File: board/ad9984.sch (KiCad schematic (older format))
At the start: 39 parts, among them P401 AD9984 I2C, U401 AD9984

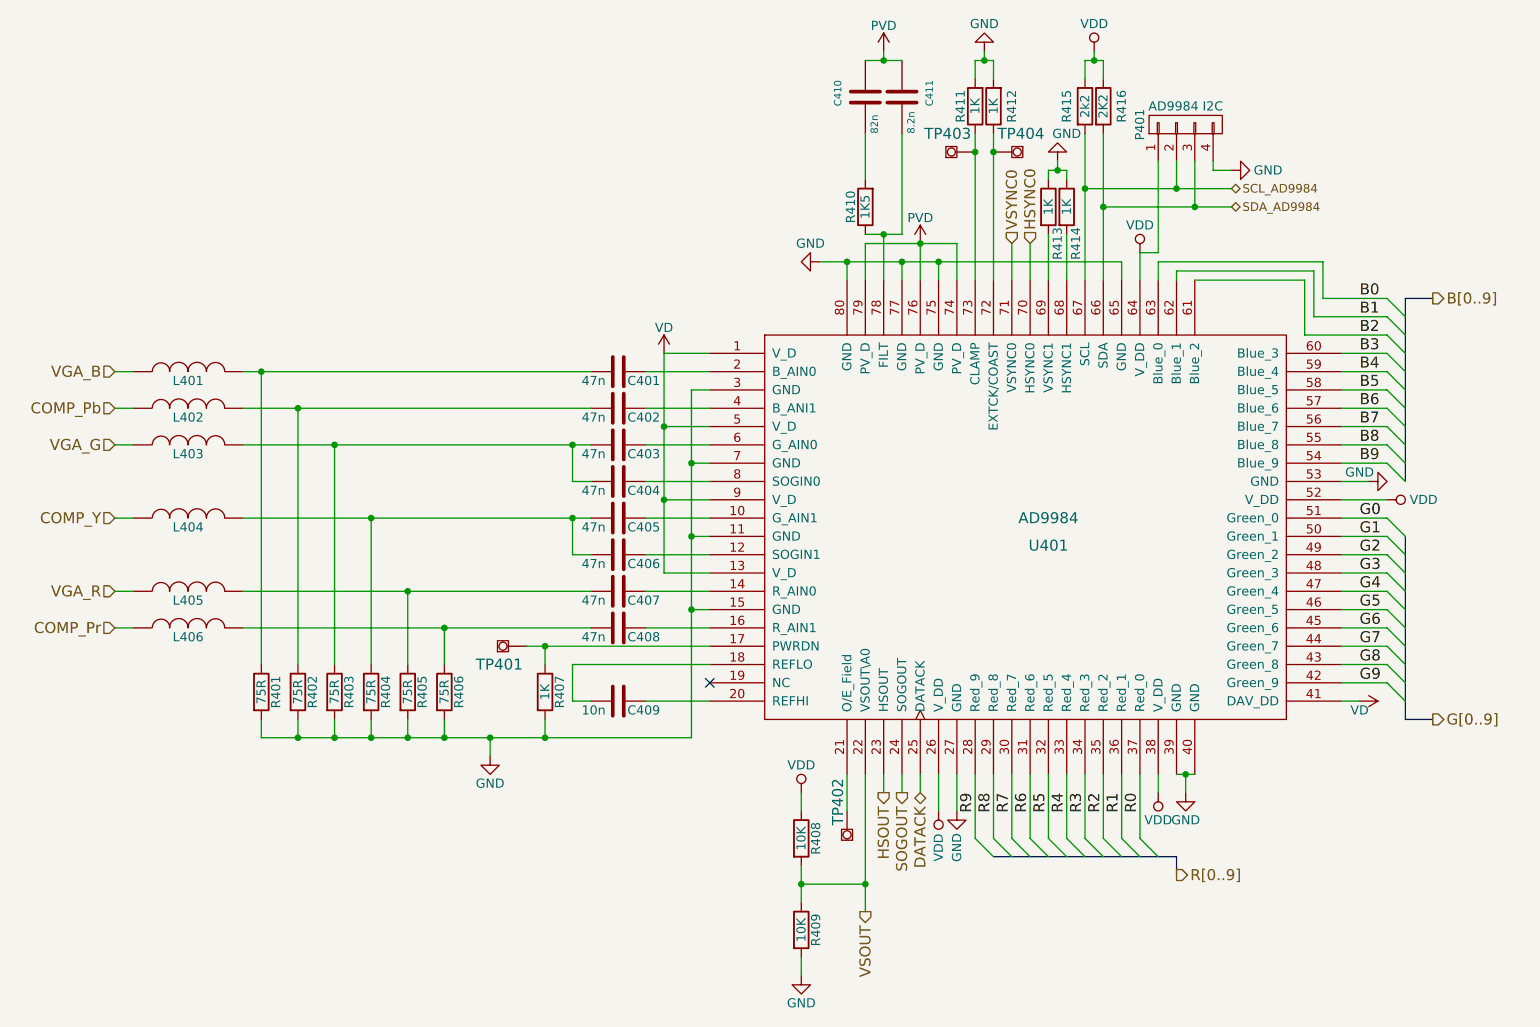
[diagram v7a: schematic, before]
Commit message: Remove component input to allow design to fit on smaller and much cheaper board
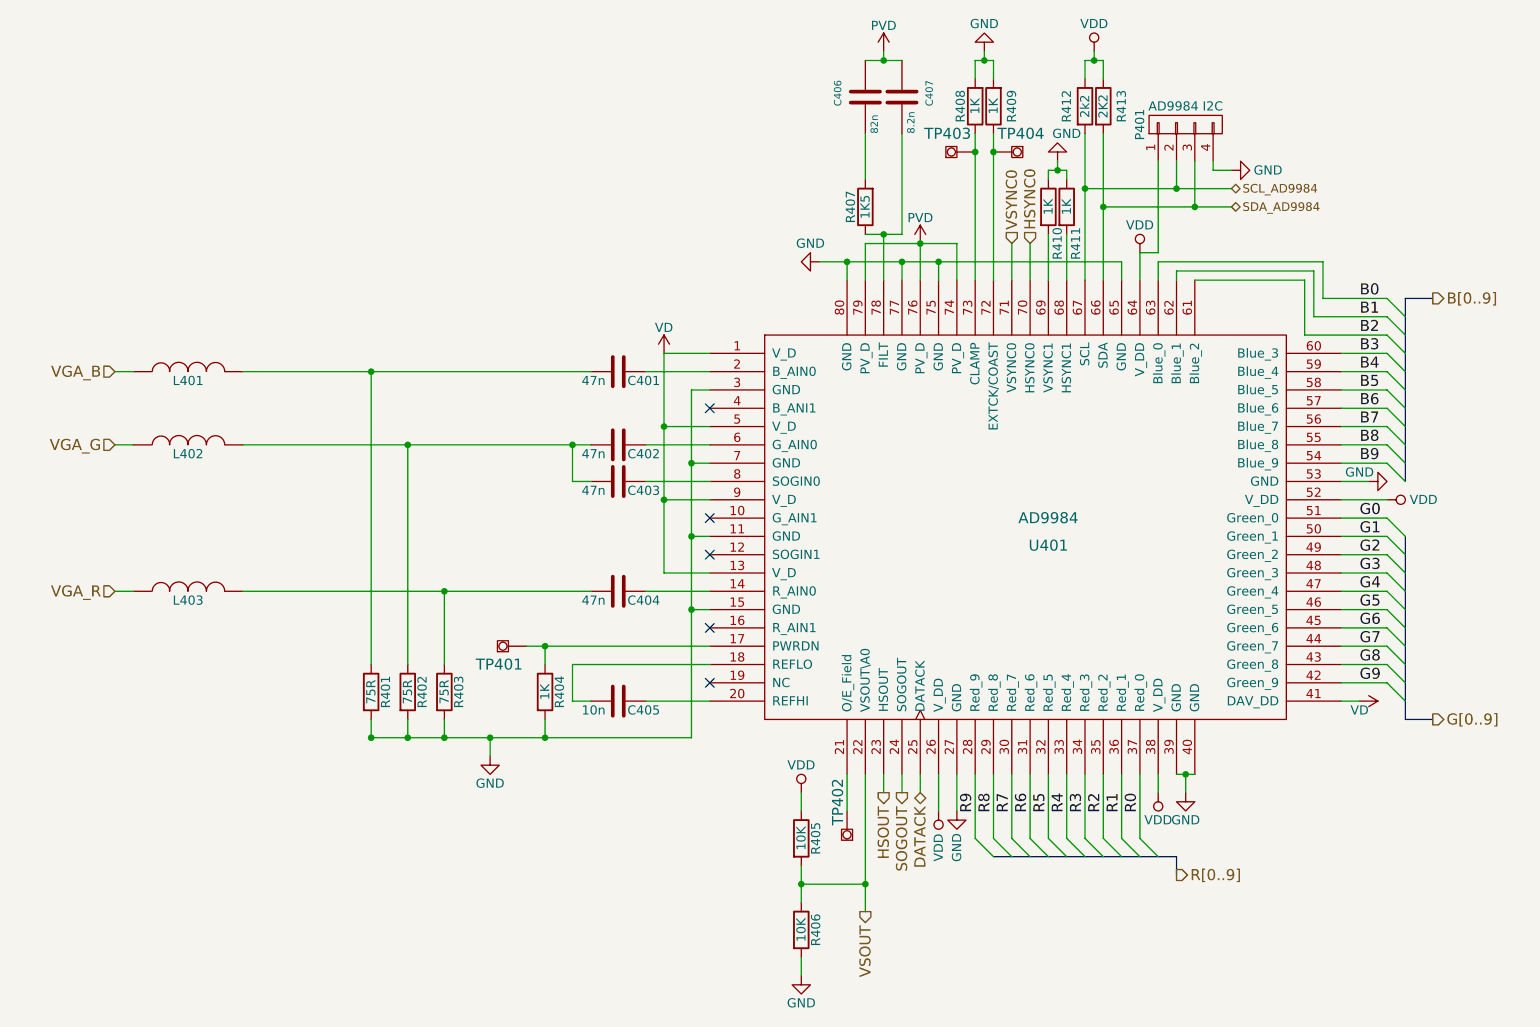
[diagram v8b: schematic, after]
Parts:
- removed C402, C405, C406, C408: 47n, Resistors_SMD:R_0805_HandSoldering, symbol C
- removed L402, L404, L406: FERRITE, Resistors_SMD:R_0805_HandSoldering, symbol INDUCTOR
- removed R401, R402, R403: 75R, Resistors_SMD:R_0805_HandSoldering, symbol R
- renumbered C403 to C402, C404 to C403, C407 to C404, C409 to C405, C410 to C406, C411 to C407, L403 to L402, L405 to L403, R404 to R401, R405 to R402, R406 to R403, R407 to R404, R408 to R405, R409 to R406, R410 to R407, R411 to R408, R412 to R409, R413 to R410, R414 to R411, R415 to R412, R416 to R413
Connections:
- net at C402.2, C403.2, L402.2: now also R402.1
- net at R401.1: now also C401.2, L401.2
- net at C404.2, L403.2: now also R403.1; no longer R402.1
- no-connect marks 1 -> 5
